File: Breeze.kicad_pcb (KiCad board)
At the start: 2 copper layers, 210.6 x 114.9 mm, 102 parts, among them J1 PJ-320A, SW1 CHOCXHSPCB-1U, SW10 CHOCXHSPCB-1U, SW11 CHOCXHSPCB-1U, SW12 CHOCXHSPCB-1U, SW13 CHOCXHSPCB-1U, SW14 CHOCXHSPCB-1U, SW15 CHOCXHSPCB-1U, SW16 CHOCXHSPCB-1U, SW17 CHOCXHSPCB-1U, SW18 CHOCXHSPCB-1U, SW19 CHOCXHSPCB-1U, SW2 CHOCXHSPCB-1U, SW20 CHOCXHSPCB-1U, SW21 CHOCXHSPCB-1U, SW22 CHOCXHSPCB-1U, SW23 CHOCXHSPCB-1U, SW24 CHOCXHSPCB-1U, SW3 CHOCXHSPCB-1U, SW4 CHOCXHSPCB-1U, SW5 CHOCXHSPCB-1U, SW6 CHOCXHSPCB-1U, SW7 CHOCXHSPCB-1U, SW8 CHOCXHSPCB-1U, SW9 CHOCXHSPCB-1U

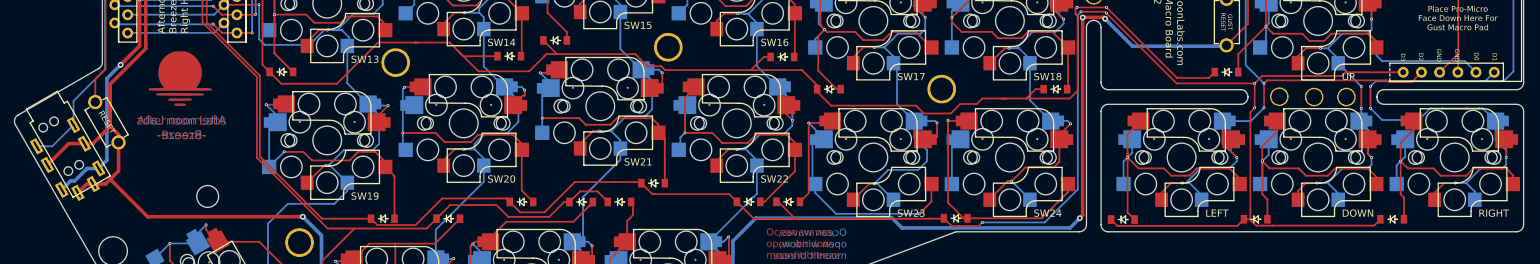
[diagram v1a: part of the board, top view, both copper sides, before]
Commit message: Switch interconnect TRRS to USB-C, change to SMD reset button (rerouting of traces not done)
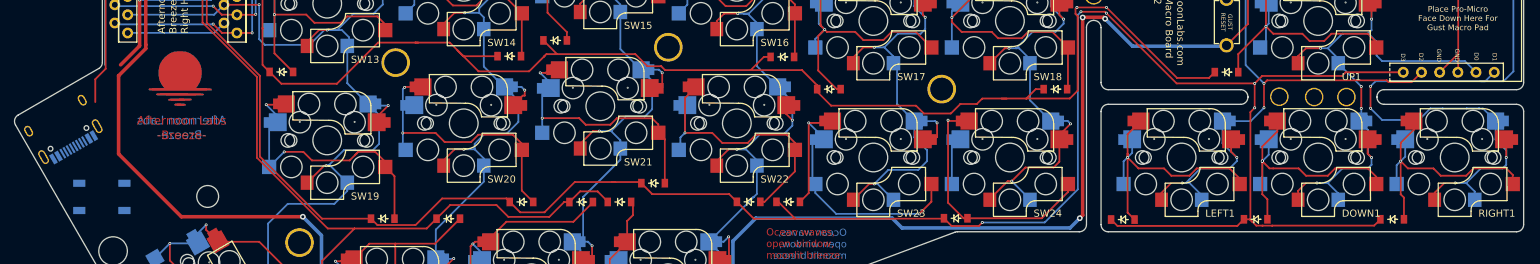
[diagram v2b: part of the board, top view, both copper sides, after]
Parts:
- removed J1: PJ-320A, Breeze:MJ-4PP-9
- added USB1: HRO-TYPE-C-31-M-12, Connector_USB:USB_C_Receptacle_HRO_TYPE-C-31-M-12, B.Cu at (108.9, 162.8)
- RSW1: footprint Breeze:TACT_SWITCH_TVBP06 -> Button_Switch_SMD:SW_SPST_TL3342; moved to B.Cu
- moved RSW1 10.4 mm to (114.9, 173.2), turned to 180 degrees
- renumbered DOWN to DOWN1, LEFT to LEFT1, RIGHT to RIGHT1, UP to UP1
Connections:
- MCU-MACRO1 pad 10: Net-(MCU-MACRO1-Pad10) -> unconnected-(MCU-MACRO1-VCC-Pad10)
- MCU-MACRO1 pad 7: Net-(MCU-MACRO1-Pad7) -> unconnected-(MCU-MACRO1-RAW-Pad7)
- MCU-MAIN1 pad 1: Net-(MCU-MAIN1-Pad1) -> DATA2
- MCU-MAIN1 pad 13: Net-(MCU-MAIN1-Pad13) -> unconnected-(MCU-MAIN1-D10(PB6)-Pad13)
- MCU-MAIN1 pad 2: DATA -> DATA1
- MCU-MAIN1 pad 24: Net-(MCU-MAIN1-Pad24) -> unconnected-(MCU-MAIN1-RAW-Pad24)
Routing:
- net DATA: track 65.2 -> 0.00 mm, vias 1 -> 0
- net DATA1: track 0.00 -> 48.6 mm, vias 0 -> 1
- net GND: track 408.5 -> 383.1 mm
- net VCC: track 74.8 -> 52.7 mm, vias 3 -> 2
- net Net-(MCU-MAIN1-Pad1): track 17.0 -> 0.00 mm, vias 1 -> 0
- net DATA2: track 0.00 -> 17.0 mm, vias 0 -> 1
- net unconnected-(MCU-MAIN1-D10(PB6)-Pad13): track 0.00 -> 14.7 mm
- net Net-(MCU-MAIN1-Pad13): track 14.7 -> 0.00 mm
- net unconnected-(MCU-MAIN1-RAW-Pad24): track 0.00 -> 14.4 mm
- net Net-(MCU-MAIN1-Pad24): track 14.4 -> 0.00 mm
